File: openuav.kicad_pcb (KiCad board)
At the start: 4 copper layers, 36 x 36 mm, 75 parts, among them J1 Conn_01x01, J10 Conn_01x01, J11 Conn_01x01, J12 Conn_01x01, J13 Conn_01x01, J14 Conn_01x01, J15 Conn_01x01, J16 Conn_01x01, J17 Conn_01x01, J18 Conn_01x01, J19 Conn_01x01, J2 Conn_01x01, J20 Conn_01x01, J21 Conn_01x01, J22 Conn_01x01, J23 Conn_01x01, J24 Conn_01x01, J25 Conn_01x01, J26 Conn_01x01, J27 Conn_01x01, J28 Conn_01x01, J29 Conn_01x01, J3 Conn_01x01, J30 Conn_01x01, J31 Conn_01x01, J32 Conn_01x01, J33 Conn_01x01, J34 Conn_01x01, J35 Conn_01x01, J36 Conn_01x01, J37 Conn_01x01, J4 Conn_01x01, J5 Conn_01x01, J6 Conn_01x01, J7 Conn_01x01, J8 Conn_01x01, J9 Conn_01x01, J99 USB_C_Receptacle_USB2.0, U1 STM32G431CBUx, U2 BMI270, U3 BMP280, U5 TPS54202DDC, U6 W25N01GVZEIG, U7 XC6206P332MR

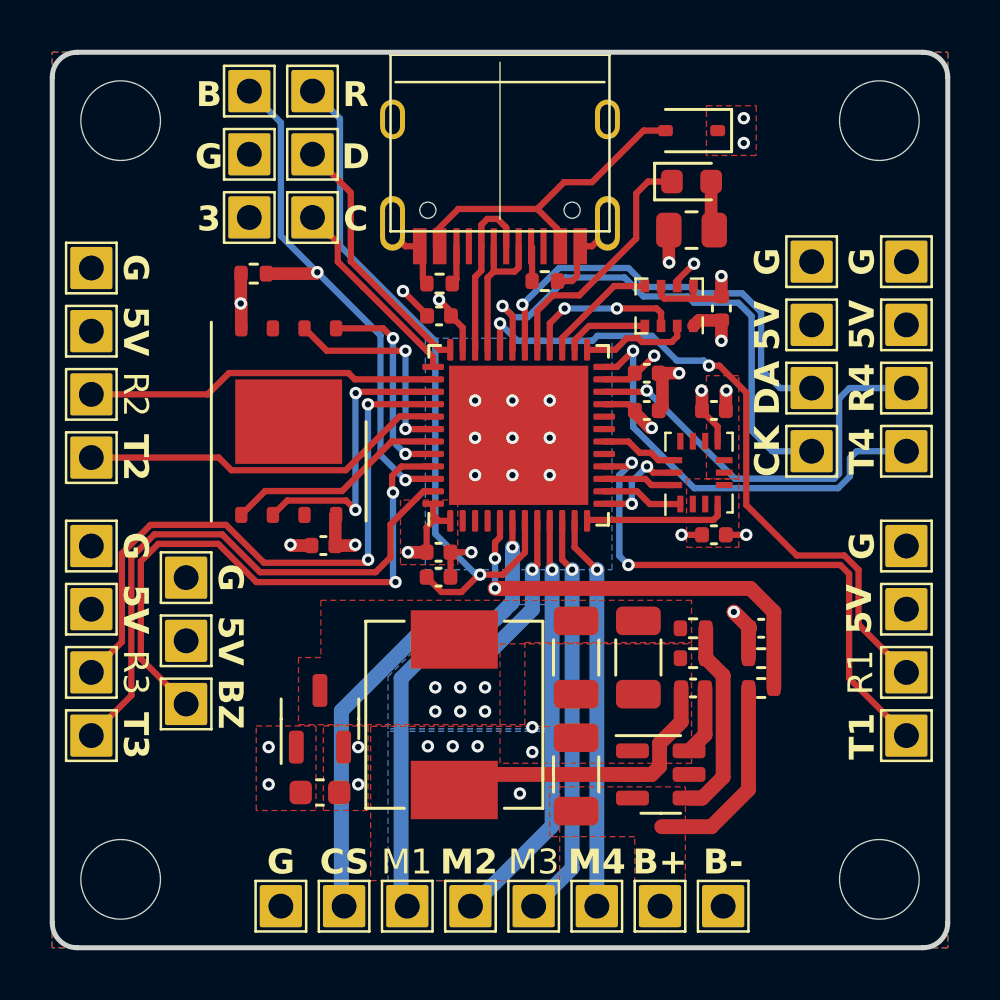
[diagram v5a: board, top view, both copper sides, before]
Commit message: Increase all vias to 0.3/0.5
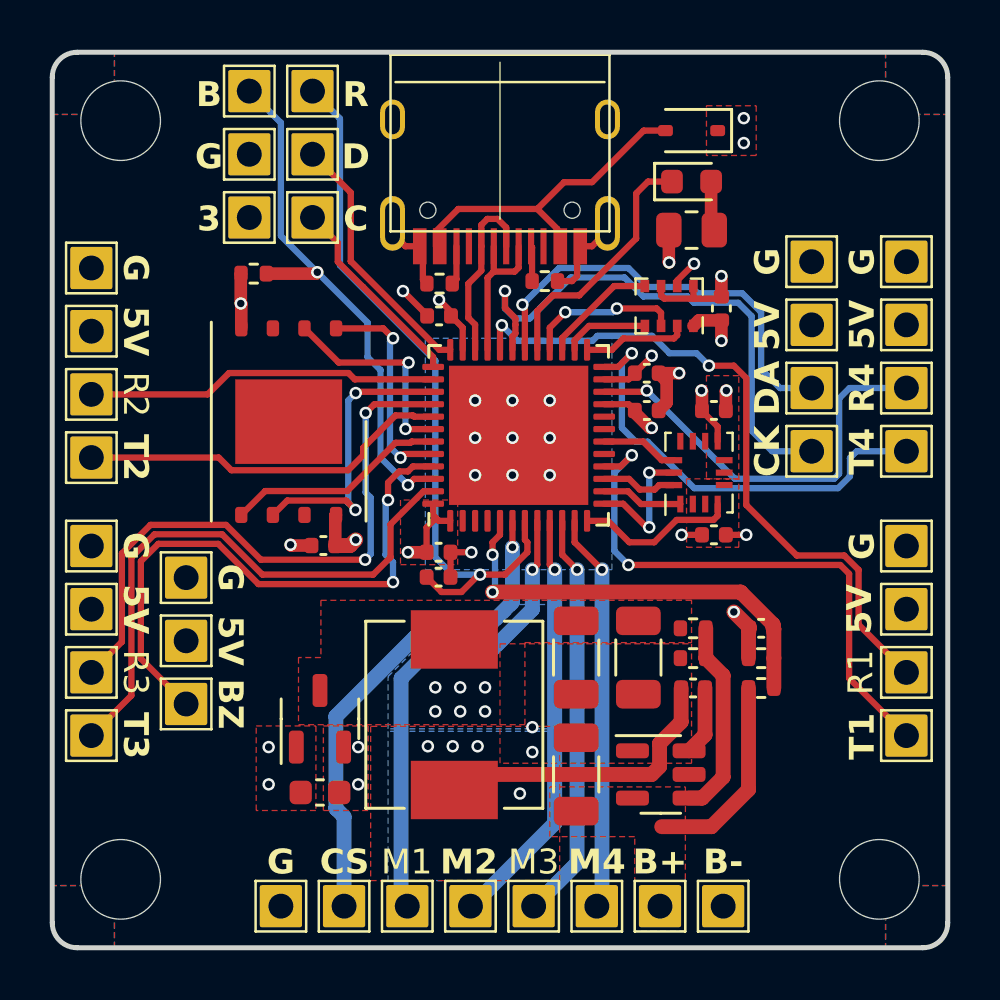
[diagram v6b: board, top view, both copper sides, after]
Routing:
- net SPI1_CLK: track 4.05 -> 5.39 mm
- net I2C_CLK: track 20.9 -> 22.1 mm
- net GYRO_INT: track 5.81 -> 6.52 mm
- net NRST: track 28.5 -> 29.1 mm
- net UART_1_TX: track 22.1 -> 22.7 mm

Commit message: continue g474 redesign
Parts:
- removed J32, J33, J34, J35, J36, J37: Conn_01x01, Connector_Custom_Pads:TP-2.54
- removed REF**: OSHW-Logo2_7.3x6mm_SilkScreen, Symbol:OSHW-Logo2_7.3x6mm_SilkScreen
- U1: value STM32G431CBUx -> STM32G474CETx; footprint Package_DFN_QFN:QFN-48-1EP_7x7mm_P0.5mm_EP5.6x5.6mm -> Package_QFP:LQFP-48_7x7mm_P0.5mm
- moved J18 67.9 mm to (92.7, 63.2)
- moved R6 61.8 mm to (97.6, 85.1), turned to 0 degrees
- moved R5 61.3 mm to (97.6, 83.1)
- moved R4 58.5 mm to (97.6, 81.2), turned to 0 degrees
- moved R3 58.4 mm to (97.6, 79.2)
- moved C8 57.1 mm to (101.9, 80.8)
- moved R2 55.2 mm to (97.6, 77.2)
- moved C7 54.4 mm to (101.9, 78.8)
- moved C12 54.1 mm to (104.8, 74.9), turned to 0 degrees
- moved C14 54.0 mm to (104.8, 78.8), turned to 0 degrees
- moved C6 53.4 mm to (101.9, 76.9)
- moved D1 52.8 mm to (114.0, 85.6), turned to 0 degrees
- moved C11 51.9 mm to (104.8, 72.9), turned to 0 degrees
- moved C10 51.2 mm to (104.8, 71.0), turned to 0 degrees
- moved R1 50.5 mm to (97.6, 75.2), turned to 0 degrees
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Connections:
- J28 pad 1: BOOT0 -> +5V
- J29 pad 1: +3V3 -> BUZZER
- J30 pad 1: SWCLK -> +BATT
- J31 pad 1: NRST -> GND
- U1 pad 10: PWM_3 -> UART_4_TX
- U1 pad 11: PWM_4 -> UART_4_RX
- U1 pad 12: GYRO_INT -> SPI1_CS
- U1 pad 16: UART_1_TX -> PWM_3
- U1 pad 17: unconnected-(U1-PB0-Pad17) -> PWM_4
- U1 pad 18: SPI1_CS -> unconnected-(U1-PB2-Pad18)
- U1 pad 19: unconnected-(U1-PB2-Pad19) -> GND
- U1 pad 2: unconnected-(U1-PC13-Pad2) -> BUZZER
- U1 pad 22: UART_4_RX -> UART_3_TX
- U1 pad 23: +3V3 -> GND
- U1 pad 24: UART_4_TX -> +3V3
- U1 pad 25: SPI2_CS -> UART_3_RX
- U1 pad 26: SPI2_CLK -> SPI2_CS
- U1 pad 27: SPI2_MISO -> SPI2_CLK
- U1 pad 28: SPI2_MOSI -> SPI2_MISO
- U1 pad 29: LED -> SPI2_MOSI
- U1 pad 32: UART_1_RX -> unconnected-(U1-PA10-Pad32)
- U1 pad 35: +3V3 -> GND
- U1 pad 36: SWDIO -> +3V3
- U1 pad 37: SWCLK -> SWDIO
- U1 pad 38: UART_2_RX -> UART_2_TX
- U1 pad 39: SPI3_CLK -> UART_2_RX
- U1 pad 40: UART_3_RX -> SPI3_CLK
- U1 pad 41: UART_2_TX -> SPI3_MISO
- U1 pad 42: SPI3_MISO -> SPI3_MOSI
- U1 pad 43: SPI3_MOSI -> UART_1_TX
- U1 pad 44: SPI3_CS -> UART_1_RX
- U1 pad 45: BUZZER -> BOOT0
- U1 pad 46: BOOT0 -> SPI3_CS
- U1 pad 47: UART_3_TX -> GND
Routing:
- net NRST: track 29.1 -> 0.00 mm, vias 1 -> 0
- net UART_1_RX: track 27.5 -> 0.00 mm, vias 2 -> 0
- net UART_3_RX: track 25.1 -> 0.00 mm, vias 2 -> 0
- net BUZZER: track 23.9 -> 0.00 mm, vias 2 -> 0
- net UART_3_TX: track 23.2 -> 0.00 mm
- net GND: track 23.1 -> 0.00 mm, vias 23 -> 0
- net UART_1_TX: track 22.7 -> 0.00 mm, vias 2 -> 0
- net I2C_CLK: track 22.1 -> 0.00 mm, vias 1 -> 0
- net BOOT0: track 21.7 -> 0.00 mm, vias 2 -> 0
- net +3V3: track 21.4 -> 0.00 mm, vias 11 -> 0
- net CURRENT: track 20.0 -> 0.00 mm, vias 1 -> 0
- net PWM_1: track 19.3 -> 0.00 mm, vias 1 -> 0
- net UART_4_TX: track 18.0 -> 0.00 mm, vias 1 -> 0
- net VOLTAGE: track 17.5 -> 0.00 mm, vias 2 -> 0
- net I2C_SDA: track 17.4 -> 0.00 mm, vias 1 -> 0
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- removed copper zone on B.Cu, net (none)
- removed copper zone on F.Cu, net (none)
- removed copper zone on F.Cu, net +3V3
- removed copper zone on In2.Cu, net +3V3
- removed copper zone on B.Cu, net +5V
- removed copper zone on F.Cu, net +5V
- removed copper zone on F.Cu, net +BATT
- removed copper zone on B.Cu, net GND
- removed copper zone on F.Cu, net GND
- removed copper zone on B.Cu, net Net-(U5-SW)
- removed copper zone on F.Cu, net Net-(U5-SW)
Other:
- outline, holes or cut-outs redrawn
- board text removed: "3"
- board text removed: "5V"
- board text removed: "B"
- board text removed: "B+"
- board text removed: "B-"
- board text removed: "BZ"
- board text removed: "C"
- board text removed: "CK"
- board text removed: "CS"
- board text removed: "D"
- board text removed: "DA"
- board text removed: "G"
- board text removed: "JLCJLCJLCJLC"
- board text removed: "M1"
- board text removed: "M2"
- board text removed: "M3"
- board text removed: "M4"
- board text removed: "R"
- board text removed: "R1"
- board text removed: "R2"
- board text removed: "R3"
- board text removed: "R4"
- board text removed: "T1"
- board text removed: "T2"
- board text removed: "T3"
- board text removed: "T4"
- board text removed: "v0.1"

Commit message: continued work on G474 board
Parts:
- added C16: 100n, Capacitor_SMD:C_0402_1005Metric, F.Cu at (140.1, 60.9)
- added U4: W25Q128JVS, Package_SO:SOIC-8_5.23x5.23mm_P1.27mm, F.Cu at (4.67, 2.88)
- L1: footprint Inductor_SMD:L_Sunlord_MWSA0603S -> Inductor_SMD:L_Sunlord_MWSA0402S
- moved C8 59.5 mm to (158.1, 61.2), turned to -90 degrees
- moved C5 55.9 mm to (156.6, 63.4)
- moved C4 55.3 mm to (156.6, 64.9)
- moved C13 54.2 mm to (156.0, 59.2)
- moved C11 54.0 mm to (158.1, 64.5), turned to 90 degrees
- moved C12 52.1 mm to (156.6, 69.8), turned to 180 degrees
- moved C7 47.3 mm to (146.0, 61.7), turned to 180 degrees
- moved C6 44.5 mm to (146.0, 70.5), turned to 180 degrees
- moved R6 9.16 mm to (89.1, 81.8)
- moved R8 8.04 mm to (89.6, 87.0)
- moved R2 6.72 mm to (91.6, 74.2)
- moved C14 6.32 mm to (109.1, 74.2)
- moved R3 5.14 mm to (92.8, 77.4)
- moved R4 4.74 mm to (92.9, 81.0)
- moved C9 4.37 mm to (105.7, 88.7)
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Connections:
- U1 pad 18: unconnected-(U1-PB2-Pad18) -> GYRO_INT
- U1 pad 32: unconnected-(U1-PA10-Pad32) -> LED
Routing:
- net SPI3_MOSI: track 0.00 -> 22.4 mm
- net +3V3: track 0.00 -> 21.0 mm, vias 0 -> 6
- net GND: track 0.00 -> 18.3 mm, vias 0 -> 15
- net SPI3_MISO: track 0.00 -> 8.74 mm
- net SPI3_CS: track 0.00 -> 8.66 mm
- net SPI1_CS: track 0.00 -> 8.03 mm, vias 0 -> 2
- net GYRO_INT: track 0.00 -> 6.87 mm, vias 0 -> 2
- net SPI2_MOSI: track 0.00 -> 6.17 mm
- net SPI3_CLK: track 0.00 -> 6.03 mm
- net SPI2_CS: track 0.00 -> 5.35 mm
- net SPI2_CLK: track 0.00 -> 5.33 mm, vias 0 -> 2
- net SPI2_MISO: track 0.00 -> 4.86 mm
- net SPI1_CLK: track 0.00 -> 4.03 mm, vias 0 -> 2
- net SPI1_MISO: track 0.00 -> 2.25 mm
- net SPI1_MOSI: track 0.00 -> 1.88 mm
- added copper zone on In2.Cu, net +3V3
- removed copper zone on In2.Cu, net +5V
